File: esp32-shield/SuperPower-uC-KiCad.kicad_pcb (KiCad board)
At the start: 2 copper layers, 45.1 x 45.1 mm, 34 parts, among them J11 DNP, J5 Conn_01x14_Female, J6 Conn_01x14_Female, J9 MCU board, Q3 S8050, Q4 S8050, SW1 SKRKAEE020, U13 ESP32-WROOM32, U14 W25Q32JVSS, U4 SN74LV1T34DBV, U5 CH340C, U6 AMS1117-3.3, Y1 12MHZ

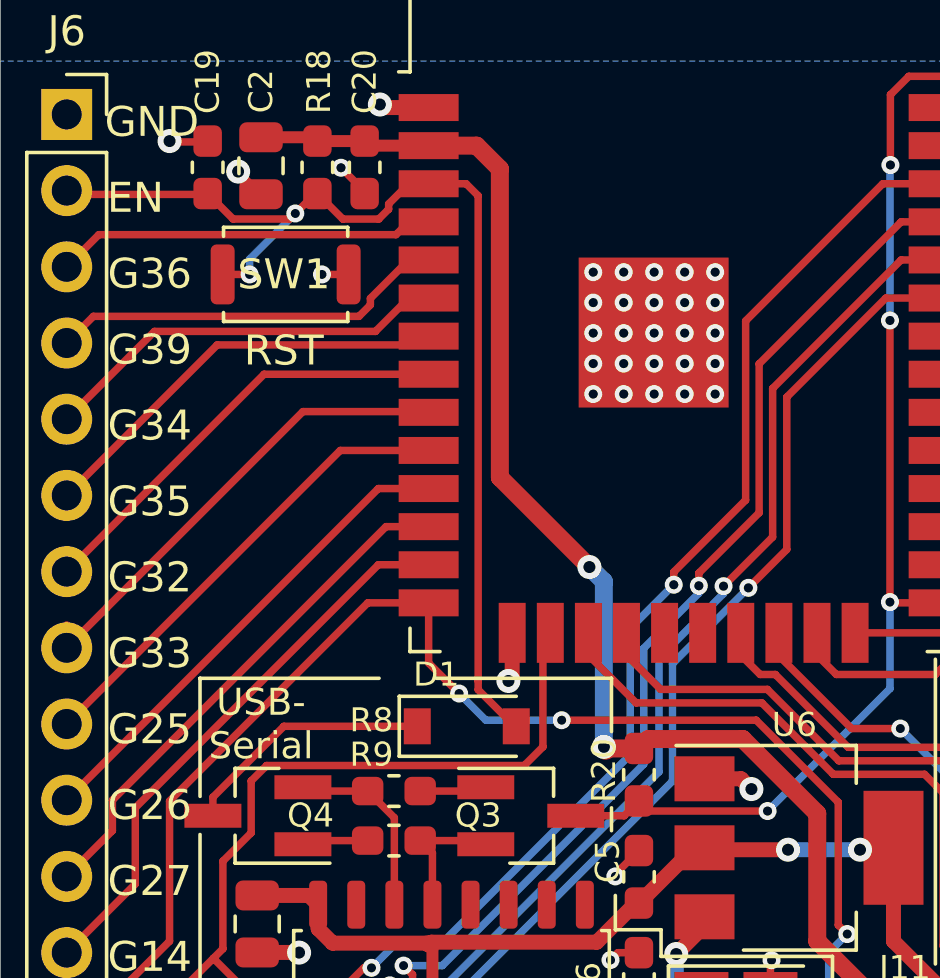
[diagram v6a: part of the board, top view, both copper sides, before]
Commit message: added another 22µ cap to 3v3mcu rail
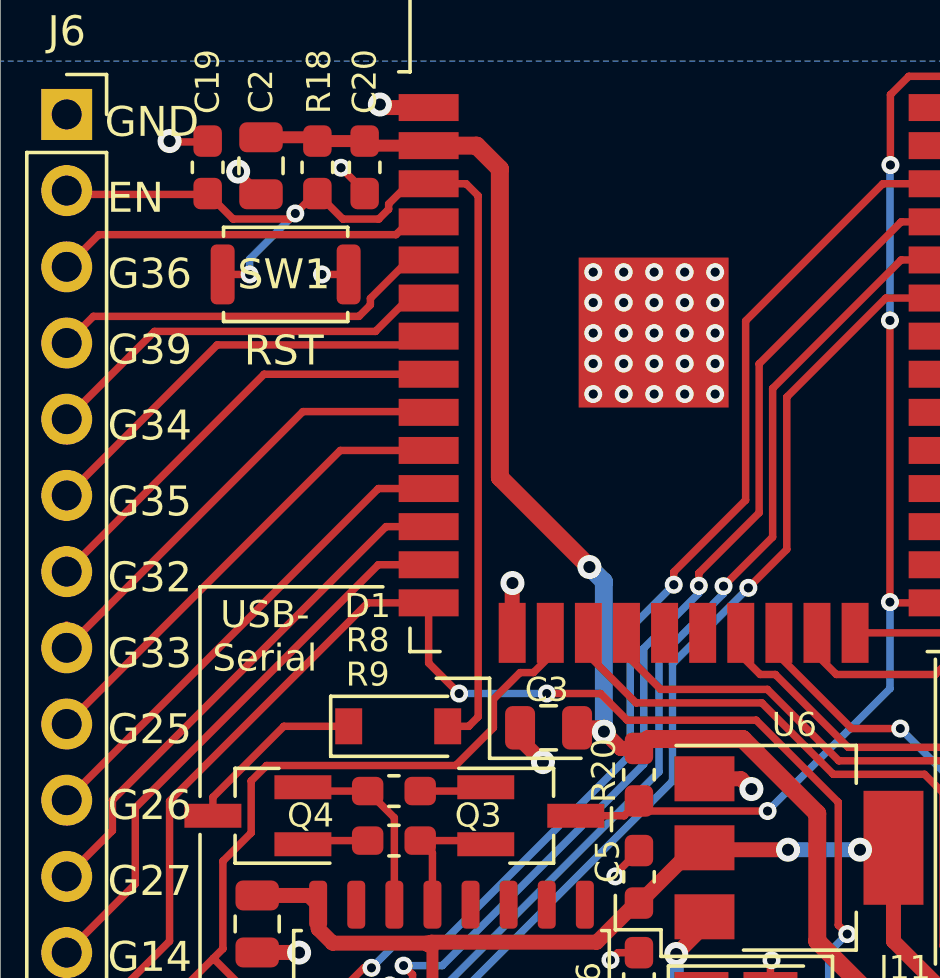
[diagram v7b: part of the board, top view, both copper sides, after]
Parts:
- added C3: 22µF, Capacitor_SMD:C_0805_2012Metric, F.Cu at (144.2, 102.0)
- moved D1 2.29 mm to (139.2, 101.9)
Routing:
- net Net-(D1-Pad1): track 8.41 -> 6.12 mm
- net GND: track 24.8 -> 26.3 mm, vias 45 -> 46
- net /EN_5v: track 46.9 -> 45.9 mm
- net /3v3_MCU: track 62.4 -> 63.0 mm

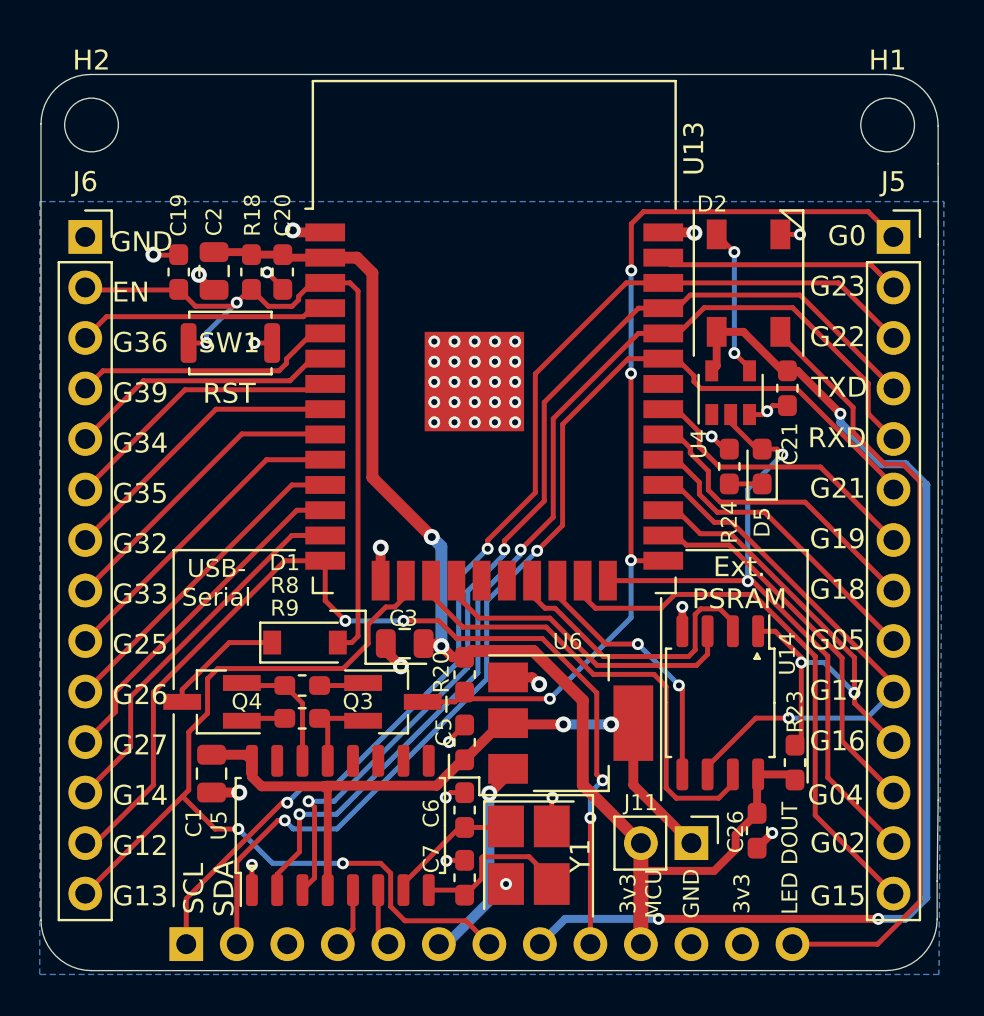
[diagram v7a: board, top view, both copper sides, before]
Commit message: changed CH340G to CH340C, deleted crystal footprint and caps, added caps
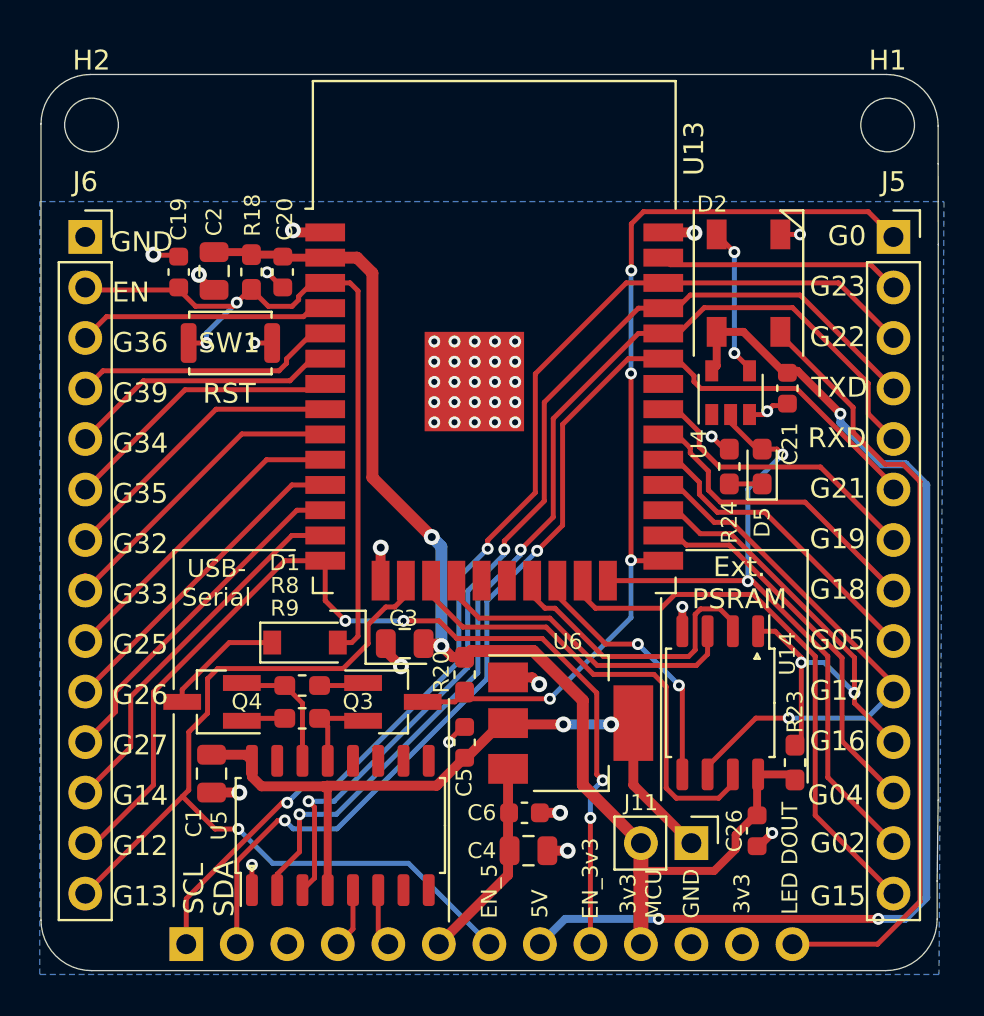
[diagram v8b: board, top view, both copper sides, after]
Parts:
- removed C7: 22pF, Capacitor_SMD:C_0603_1608Metric_Pad1.05x0.95mm_HandSolder
- removed Y1: 12MHZ, Crystal:Crystal_SMD_3225-4Pin_3.2x2.5mm_HandSoldering
- added C4: 22µF, Capacitor_SMD:C_0805_2012Metric, F.Cu at (150.4, 112.4)
- C19, C5: footprint Capacitor_SMD:C_0603_1608Metric_Pad1.05x0.95mm_HandSolder -> Capacitor_SMD:C_0603_1608Metric
- C20, C21, C26: value 0.1µF -> 1µF; footprint Capacitor_SMD:C_0603_1608Metric_Pad1.05x0.95mm_HandSolder -> Capacitor_SMD:C_0603_1608Metric
- C6: value 22pF -> 1µF; footprint Capacitor_SMD:C_0603_1608Metric_Pad1.05x0.95mm_HandSolder -> Capacitor_SMD:C_0603_1608Metric
- moved C6 3.01 mm to (150.2, 110.5), turned to 0 degrees
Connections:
- C6 pad 1: Net-(C6-Pad1) -> /VBUS
- U5 pad 7: Net-(C6-Pad1) -> Net-(U5-Pad7)
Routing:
- net Net-(U5-Pad8): track 8.75 -> 0.00 mm
- net Net-(C6-Pad1): track 6.78 -> 0.00 mm
- net GND: track 26.3 -> 24.6 mm, vias 46 -> 44
- net /EN_5v: track 45.9 -> 44.9 mm, vias 2 -> 1
- net /VBUS: track 10.3 -> 10.6 mm, vias 1 -> 0
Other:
- board text added: "EN_3v3"
- board text added: "EN_5"
